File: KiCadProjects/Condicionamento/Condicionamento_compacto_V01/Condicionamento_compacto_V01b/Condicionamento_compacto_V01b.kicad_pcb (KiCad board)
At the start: 2 copper layers, 40 x 33 mm, 19 parts, among them J1 Entrada, J2 Canais, J3 Conn_01x02, J4 Conn_01x02, U1-Cond1 AD8056ARMZ

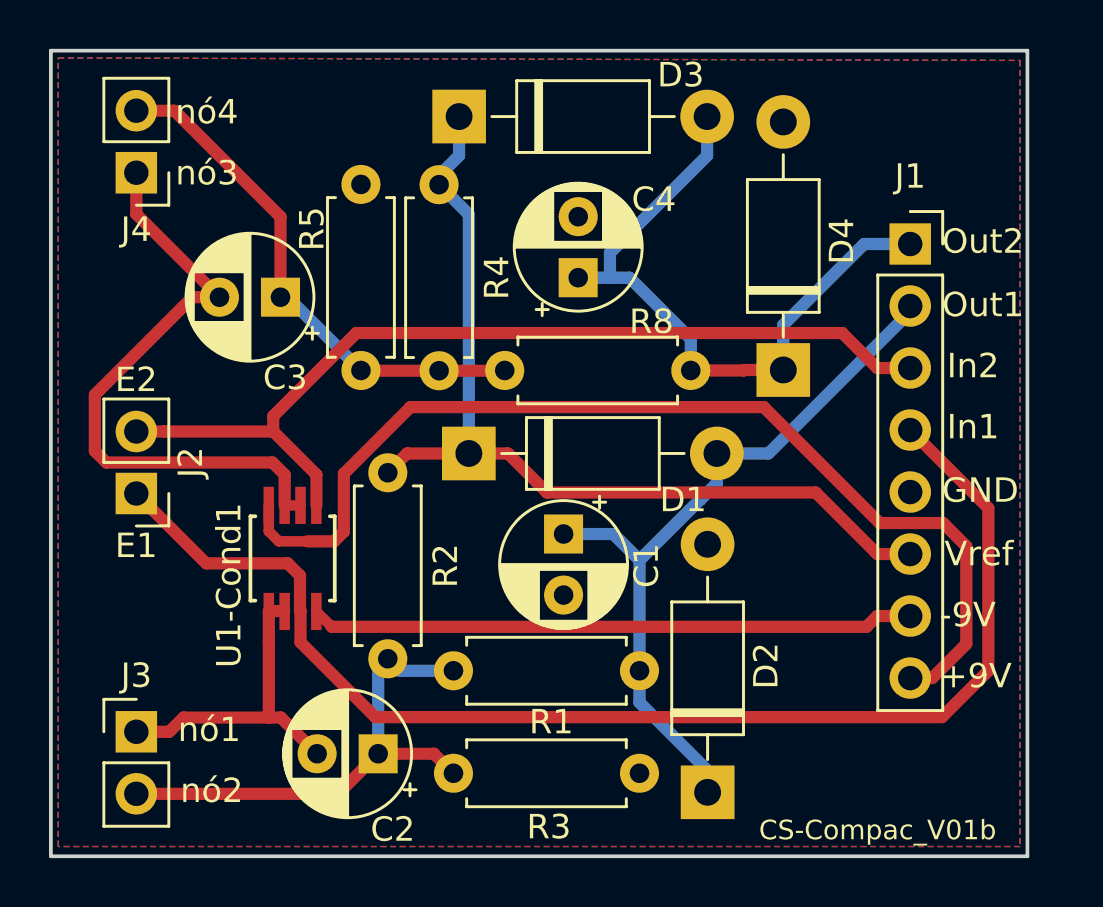
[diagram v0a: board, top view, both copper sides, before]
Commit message: V01aCopia: menor, com vias. V01a: maior, sem vias
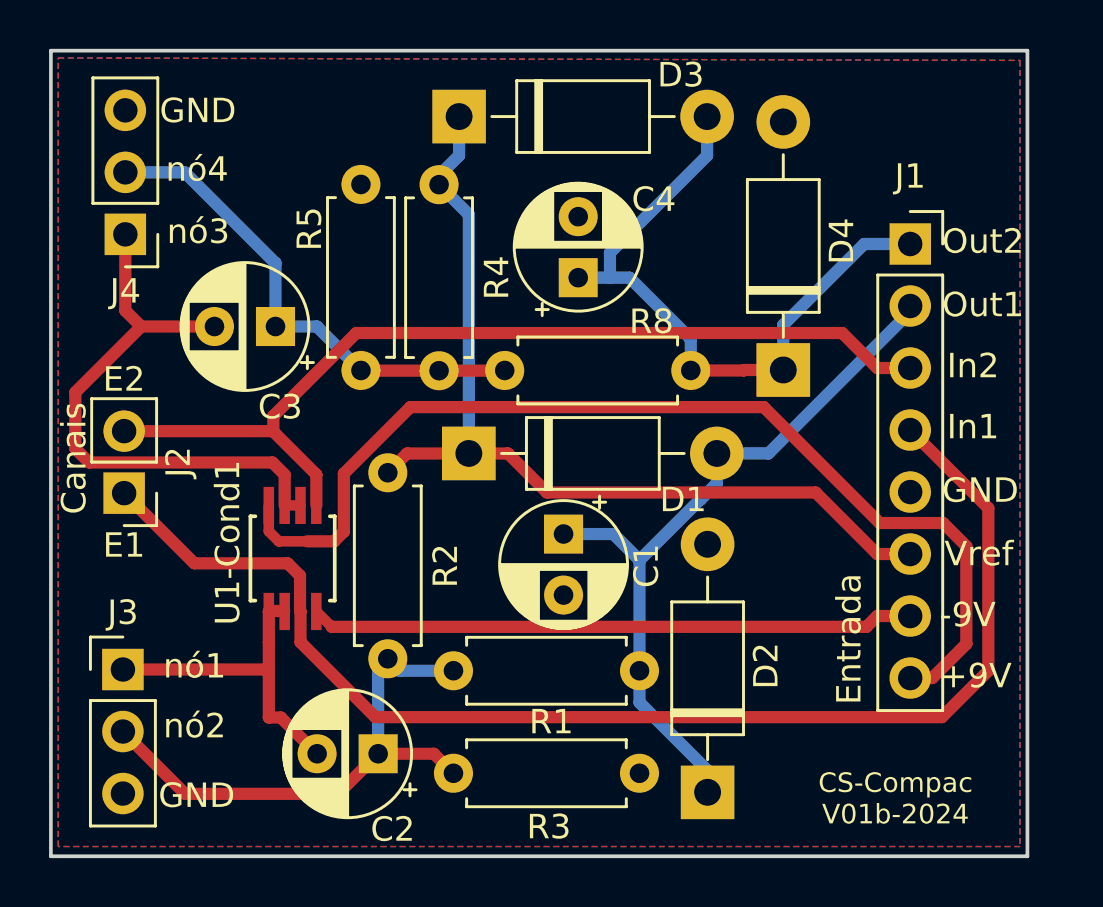
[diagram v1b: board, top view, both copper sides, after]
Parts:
- J3, J4: value Conn_01x02 -> Conn_01x03; footprint Connector_PinHeader_2.54mm:PinHeader_1x02_P2.54mm_Vertical -> Connector_PinHeader_2.54mm:PinHeader_1x03_P2.54mm_Vertical
- moved J3 2.61 mm to (130.1, 110.5)
- moved J4 2.56 mm to (130.2, 92.6)
- moved C3 1.22 mm to (136.3, 96.4)
- moved J2 0.50 mm to (130.1, 103.2)
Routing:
- net nó2: track 20.9 -> 22.6 mm
- net nó3: track 25.7 -> 24.1 mm
- net nó4: track 21.4 -> 20.4 mm
- net Canal_2: track 38.1 -> 38.6 mm
- net Canal_1: track 52.3 -> 52.8 mm
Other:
- board text added: "CS-Compac V01b-2024"
- board text removed: "CS-Compac_V01b"

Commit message: enviar para producao
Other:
- board text added: "Canais"
- board text added: "Entrada"
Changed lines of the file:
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@@
       (plot_on_all_layers_selection 0x0000000_00000000)
       (disableapertmacros false)
-      (usegerberextensions false)
-      (usegerberattributes true)
-      (usegerberadvancedattributes true)
-      (creategerberjobfile true)
+      (usegerberextensions true)
+      (usegerberattributes false)
+      (usegerberadvancedattributes false)
+      (creategerberjobfile false)
       (dashed_line_dash_ratio 12.000000)
       (dashed_line_gap_ratio 3.000000)
@@
       (psa4output false)
       (plotreference true)
-      (plotvalue true)
+      (plotvalue false)
       (plotinvisibletext false)
       (sketchpadsonfab false)
-      (subtractmaskfromsilk false)
+      (subtractmaskfromsilk true)
       (outputformat 1)
       (mirror false)
-      (drillshape 1)
+      (drillshape 0)
       (scaleselection 1)
-      (outputdirectory "")
+      (outputdirectory "gerber/")
     )
   )
@@
   (gr_line (start 127.1 118.1) (end 167.1 118.1)
     (stroke (width 0.15) (type default)) (layer "Edge.Cuts"))
+  (gr_text "CS-Compac\nV01b-2024" (at 132.9 100 -90) (layer "B.SilkS")
+    (effects (font (size 1.5 1.5) (thickness 0.15)) (justify left bottom))
+  )
+  (gr_text "Entrada" (at 164.7 100.7 90) (layer "B.SilkS")
+    (effects (font (size 1 1) (thickness 0.15)))
+  )
+  (gr_text "Canais" (at 127.8 101.8 90) (layer "B.SilkS")
+    (effects (font (size 1 1) (thickness 0.15)))
+  )
   (gr_text "GND" (at 131.55 88.15) (layer "F.SilkS")
     (effects (font (size 1 1) (thickness 0.1)) (justify left bottom))

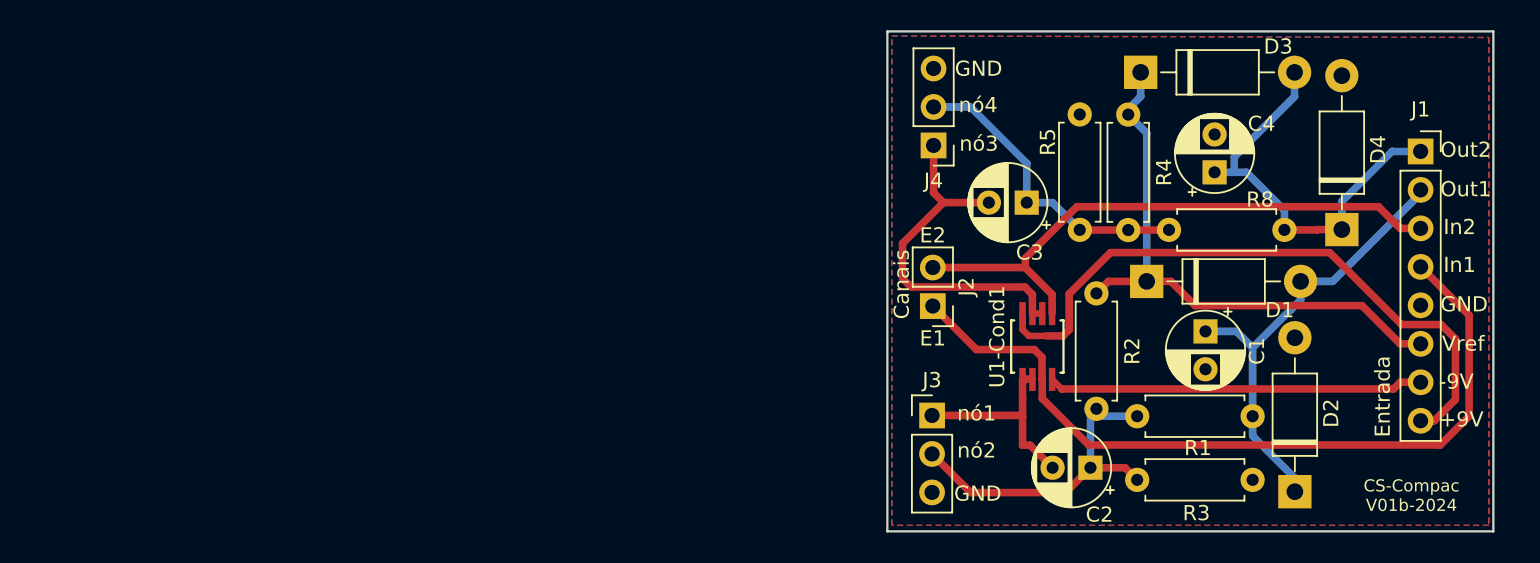
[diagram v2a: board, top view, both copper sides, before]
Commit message: mudanca de tamanho - enviado para producao
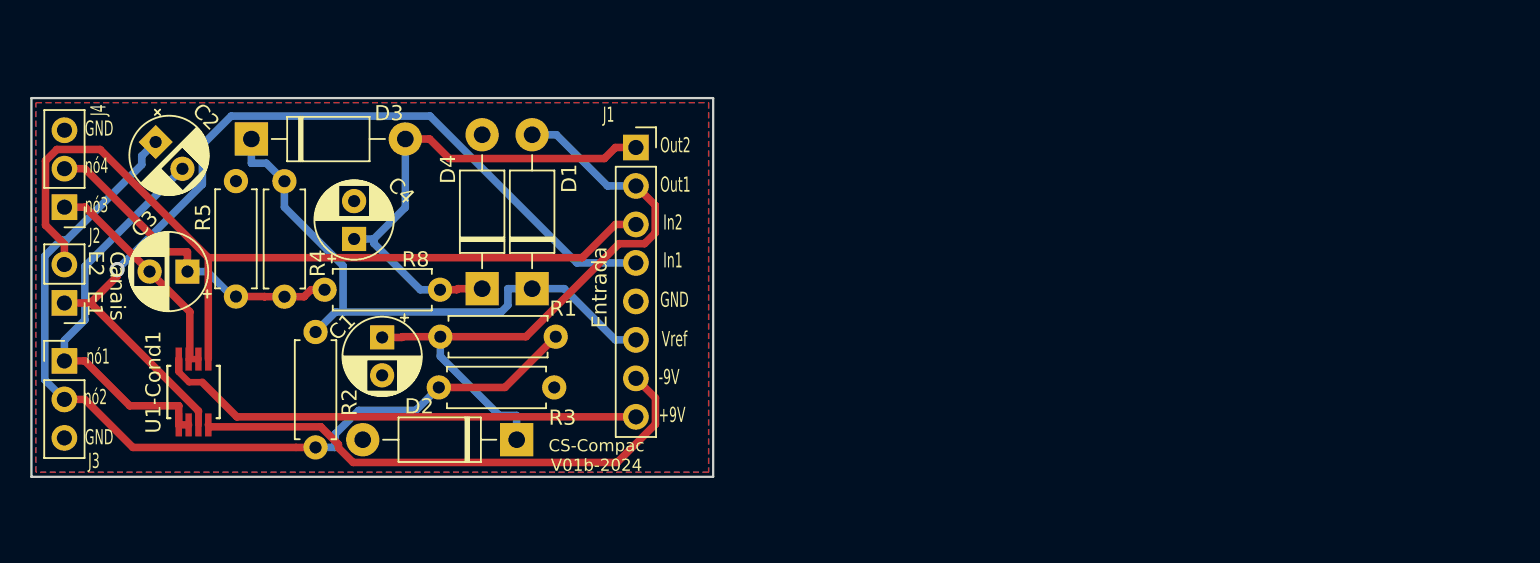
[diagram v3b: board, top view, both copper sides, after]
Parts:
- moved C2 65.3 mm to (78.8, 92.4), turned to -45 degrees
- moved D3 58.9 mm to (85.1, 92.2)
- moved J4 57.5 mm to (72.8, 96.7)
- moved J3 57.4 mm to (72.8, 106.8)
- moved J2 57.3 mm to (72.8, 103.0)
- moved C4 57.0 mm to (91.9, 98.8)
- moved D4 56.9 mm to (100.3, 102.1)
- moved R8 55.9 mm to (90.0, 102.2)
- moved R5 55.9 mm to (84.1, 102.6)
- moved R4 55.9 mm to (87.3, 95.0)
- moved U1-Cond1 55.8 mm to (81.3, 108.9)
- moved C3 55.6 mm to (80.9, 101.0)
- moved C1 54.4 mm to (93.8, 105.3)
- moved J1 51.8 mm to (110.5, 92.8)
- moved R2 51.6 mm to (89.4, 104.9)
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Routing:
- net nó2: track 22.6 -> 58.1 mm
- net Canal_2: track 38.6 -> 57.2 mm
- net nó1: track 13.6 -> 26.6 mm
- net Out_1: track 30.5 -> 42.3 mm
- net -9V: track 24.8 -> 35.3 mm
- net +9V: track 42.7 -> 32.3 mm
- net nó3: track 24.1 -> 14.9 mm
- net Canal_1: track 52.8 -> 59.6 mm, vias 0 -> 1
- net Out_2: track 27.4 -> 33.5 mm
- net nó4: track 20.4 -> 21.6 mm
- net Vref: track 38.1 -> 38.9 mm
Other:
- board size 40 x 33 mm -> 45 x 25 mm
